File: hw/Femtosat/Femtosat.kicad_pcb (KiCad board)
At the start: 2 copper layers, 61.5 x 25 mm, 26 parts, among them J1 USB_B_Micro, J2 Programmer, U0 AP7215-33YG-13, U1 SAMD21G, U2 MKRZero_Shield, U3 SD, Y1 32.768kHz

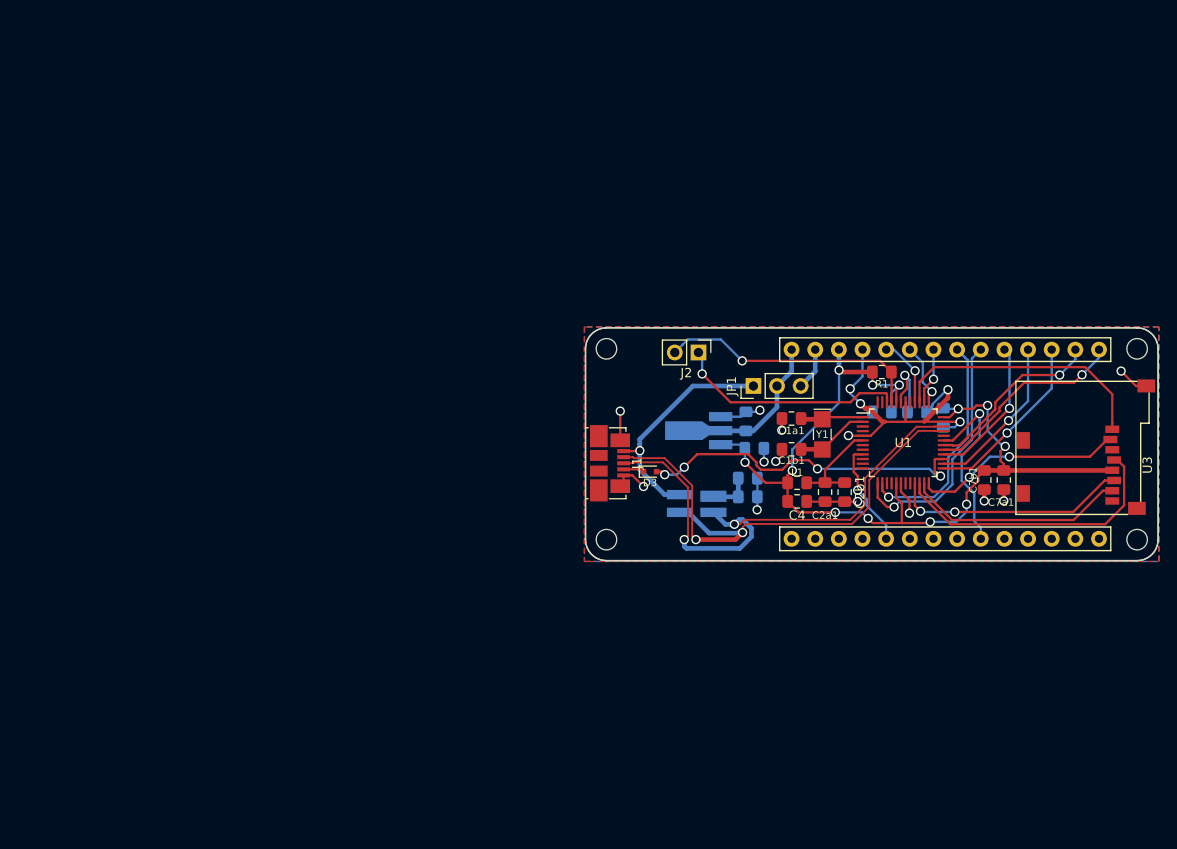
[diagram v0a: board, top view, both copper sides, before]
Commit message: Added library for certain components. Symbols and footprints were associated.
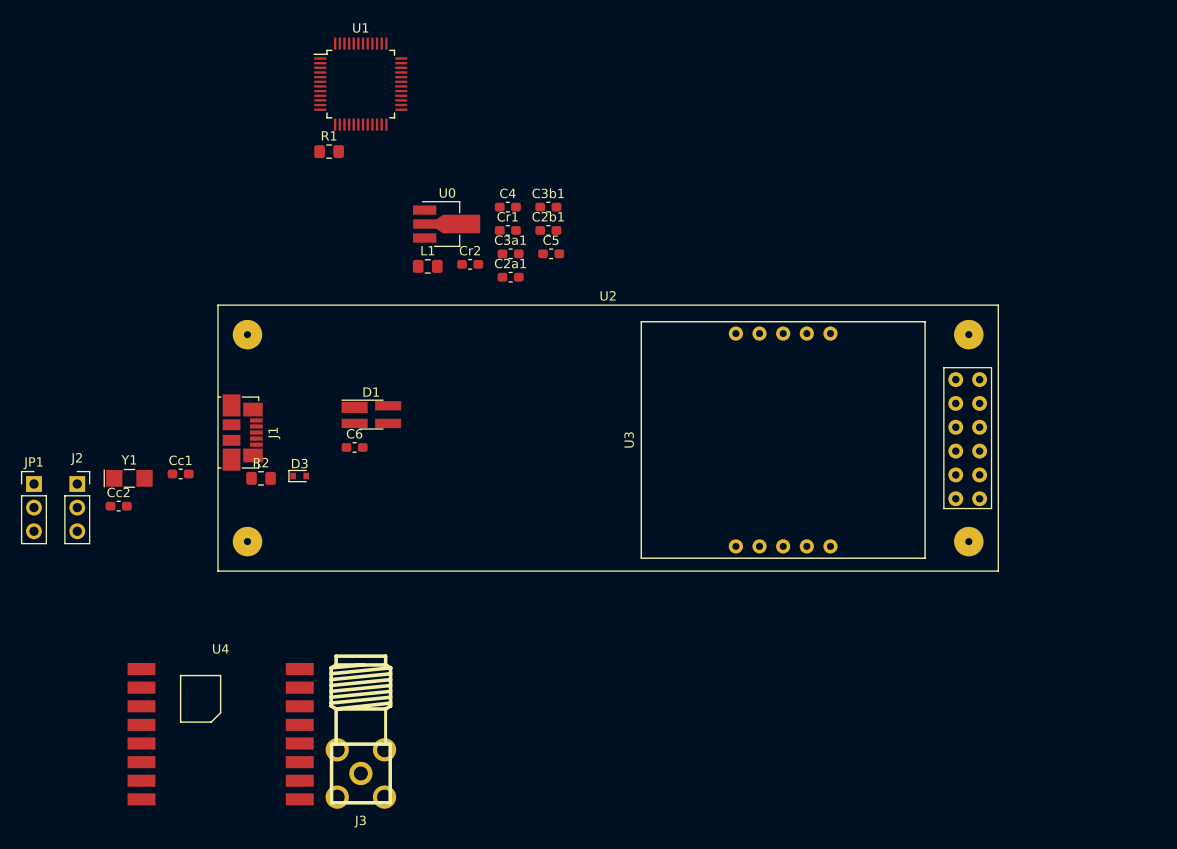
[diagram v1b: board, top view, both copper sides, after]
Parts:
- removed C1a1, C1b1: 9pF, Capacitor_SMD:C_0805_2012Metric_Pad1.15x1.40mm_HandSolder
- removed C7a1: 100nF, Capacitor_SMD:C_0805_2012Metric_Pad1.15x1.40mm_HandSolder
- removed C7b1: 10uF, Capacitor_SMD:C_0805_2012Metric_Pad1.15x1.40mm_HandSolder
- added Cc1: 9pF, Capacitor_SMD:C_0603_1608Metric_Pad1.05x0.95mm_HandSolder, F.Cu at (97.2, 71.3)
- added Cc2: 9pF, Capacitor_SMD:C_0603_1608Metric_Pad1.05x0.95mm_HandSolder, F.Cu at (90.5, 74.7)
- added J3: SMA, Antenna:SMA, F.Cu at (116.5, 103.4)
- added U4: RFM69HCW, Transceptor:RFM69HCW, F.Cu at (101.5, 99.2)
- C2a1, C2b1, C4: footprint Capacitor_SMD:C_0805_2012Metric_Pad1.15x1.40mm_HandSolder -> Capacitor_SMD:C_0603_1608Metric_Pad1.05x0.95mm_HandSolder
- C3a1, C3b1, C5, C6, Cr1, Cr2: footprint Capacitor_SMD:C_0805_2012Metric_Pad1.15x1.40mm_HandSolder -> Capacitor_SMD:C_0603_1608Metric_Pad1.05x0.95mm_HandSolder; moved to F.Cu
- D1, R2, U0: moved to F.Cu
- J2: footprint Connector_PinHeader_2.54mm:PinHeader_1x02_P2.54mm_Vertical -> Connector_PinSocket_2.54mm:PinSocket_1x03_P2.54mm_Vertical
- U2: value MKRZero_Shield -> TRH-G2; footprint MKRZero_Shield:MKRZero_Shield -> GPS:TRH-G2
- U3: value SD -> XA1110; footprint SD:microSD_socket -> GPS:XA1110
- moved JP1 78.0 mm to (81.4, 72.3), turned to 0 degrees
- moved Y1 74.6 mm to (91.7, 71.7), turned to 0 degrees
- moved U1 69.9 mm to (116.5, 29.4)
- moved J2 68.2 mm to (86.1, 72.3), turned to 0 degrees
- moved R1 63.9 mm to (113.1, 36.6)
- moved R2 52.3 mm to (105.8, 71.7)
- moved C3a1 49.7 mm to (132.6, 47.6), turned to 0 degrees
- moved L1 46.0 mm to (123.7, 49.0), turned to 0 degrees
- moved C4 44.3 mm to (132.3, 42.6)
- moved C5 42.8 mm to (137.0, 47.6)
- moved C6 42.6 mm to (115.9, 68.4)
- moved C2b1 42.5 mm to (136.7, 45.1), turned to 0 degrees
- moved C3b1 42.0 mm to (136.7, 42.6), turned to 0 degrees
- moved C2a1 40.9 mm to (132.6, 50.1), turned to 0 degrees
- moved J1 39.6 mm to (103.8, 66.8)
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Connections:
- U2 pad 1: /AREF -> /5V0
- U2 pad 10: /PIN_1 -> /RX
- U2 pad 11: /PIN_2 -> /TX
- U2 pad 12: /PIN_3 -> Net-(U2-Pad12)
- U2 pad 2: /A0 -> /5V0
- U2 pad 3: /A1 -> GND
- U2 pad 4: /A2 -> GND
- U2 pad 5: /A3 -> GND
- U2 pad 6: /A4 -> GND
- U2 pad 7: /A5 -> /GPS_RST
- U2 pad 8: /A6 -> GND
- U2 pad 9: /PIN_0 -> Net-(U2-Pad9)
- U3 pad 1: /SD_CD -> /GPS_INT
- U3 pad 10: (no net) -> /GPS_WK
- U3 pad 2: /SD_MISO -> GND
- U3 pad 3: GND -> /3V3
- U3 pad 4: /SD_SCK -> /SDA
- U3 pad 5: /3V3 -> /SCL
- U3 pad 6: /SD_MOSI -> /RX
- U3 pad 7: /SD_NSS -> /TX
- U3 pad 8: (no net) -> /GPS_PPS
- U3 pad 9: (no net) -> /GPS_RST
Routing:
- net /3V3: track 100.9 -> 0.00 mm, vias 12 -> 0
- net GND: track 71.1 -> 0.00 mm, vias 17 -> 0
- net /USB_P: track 57.0 -> 0.00 mm, vias 2 -> 0
- net /USB_N: track 55.8 -> 0.00 mm, vias 2 -> 0
- net /USB_ID: track 36.7 -> 0.00 mm, vias 4 -> 0
- net /SD_SCK: track 30.8 -> 0.00 mm
- net /SWCLK: track 28.6 -> 0.00 mm, vias 1 -> 0
- net /SD_CD: track 28.5 -> 0.00 mm
- net /SDA: track 26.7 -> 0.00 mm, vias 1 -> 0
- net /SD_MOSI: track 25.5 -> 0.00 mm, vias 2 -> 0
- net /VBUS: track 25.0 -> 0.00 mm, vias 1 -> 0
- net /SWDIO: track 24.9 -> 0.00 mm, vias 1 -> 0
- net /SCL: track 24.4 -> 0.00 mm, vias 1 -> 0
- net /SD_NSS: track 23.7 -> 0.00 mm
- net /SD_MISO: track 22.5 -> 0.00 mm, vias 2 -> 0
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- removed copper zone on B.Cu, net GND
- removed copper zone on F.Cu, net GND
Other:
- board outline removed
- net class Default: trace_width 0.5 -> 0.25; via_dia 1 -> 0.8; via_drill 0.7 -> 0.4
